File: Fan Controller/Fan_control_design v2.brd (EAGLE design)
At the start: 49.9 x 49.5 mm, 49 parts, among them Q1 IRF520, Q3 IRF520, Q4 IRF520, U1 ATMEGA328P_TQFP

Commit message: update
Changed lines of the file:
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@@
 <setting verticaltext="up"/>
 </settings>
-<grid distance="0.5" unitdist="mm" unit="mm" style="lines" multiple="1" display="yes" altdistance="0.025" altunitdist="inch" altunit="inch"/>
+<grid distance="0.0196850394" unitdist="inch" unit="inch" style="lines" multiple="1" display="yes" altdistance="0.025" altunitdist="inch" altunit="inch"/>
 <layers>
 <layer number="1" name="Top" color="4" fill="1" visible="yes" active="yes"/>
@@
 <contactref element="ISP1" pad="6"/>
 <polygon width="0.4064" layer="1">
-<vertex x="0" y="48.895"/>
+<vertex x="0" y="50.395"/>
 <vertex x="50.8" y="50.165"/>
 <vertex x="50.8" y="0.27"/>
@@
 </polygon>
 <polygon width="0.4064" layer="16">
-<vertex x="0" y="46.99"/>
-<vertex x="50.8" y="46.99"/>
+<vertex x="0" y="50.49"/>
+<vertex x="50.8" y="50.49"/>
 <vertex x="50.8" y="0"/>
 <vertex x="0" y="0"/>

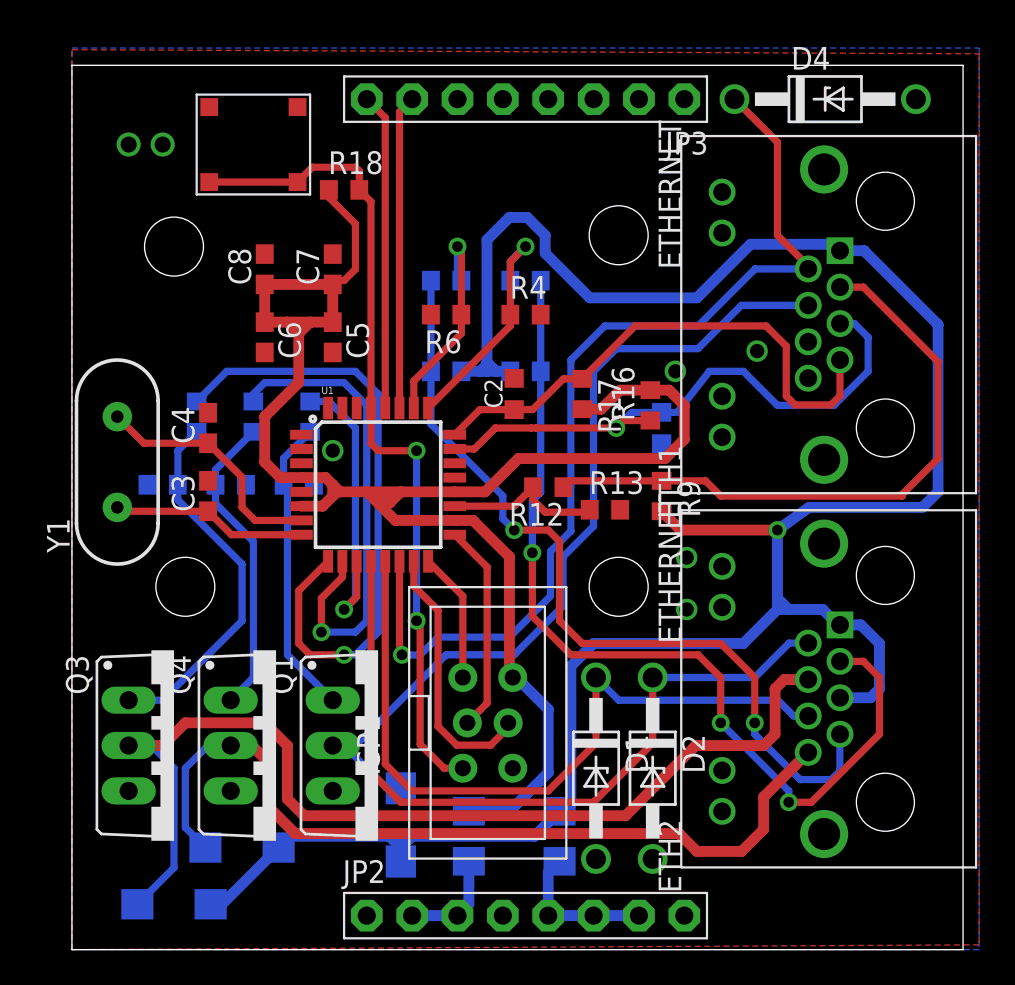
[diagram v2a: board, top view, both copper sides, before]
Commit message: cleaned up silk screens
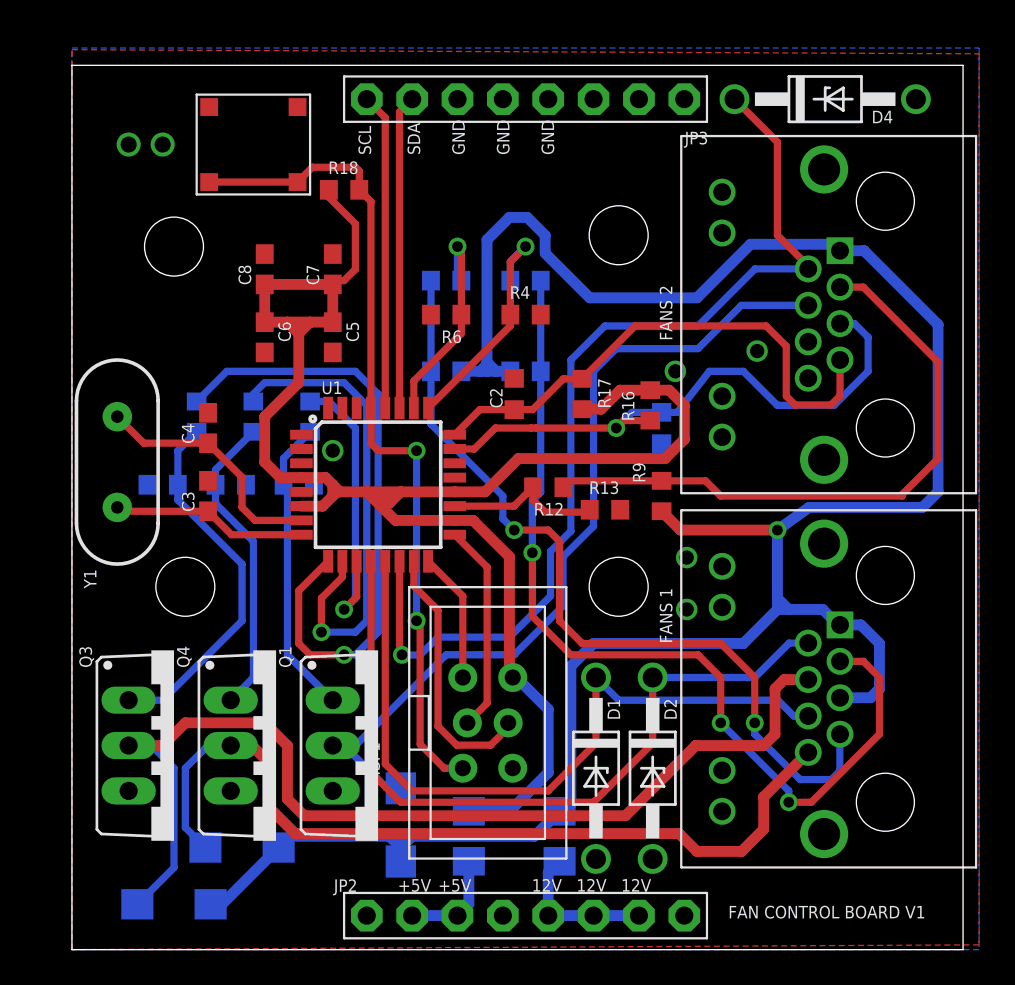
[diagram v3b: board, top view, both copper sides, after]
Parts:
- ETH1: value ETHERNET -> FANS 2
- ETH2: value ETHERNET -> FANS 1
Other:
- board text added: "+5V"
- board text added: "12V"
- board text added: "FAN CONTROL BOARD V1"
- board text added: "GND"
- board text added: "SCL"
- board text added: "SDA"
